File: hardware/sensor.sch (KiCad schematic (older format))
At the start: 55 parts, among them P1 CONN_01X05, SW1 Reset, T1 BUK9Y22, U1 LMR16006, U2 CD74HC4046, U3 CD74HC4046, U4 Atmel_SAM_D09, U5 OPA376AIDCK, X1 UART, X2 60V

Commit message: Finished routing except GND (needs plane etc pp); VCC and maybe even 3V3 needs thicker traces; Fixed missing supply cap for SAMD09 in the schema as well as some wrong footprint for SWD
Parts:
- added C6: 100n, Capacitors_SMD:C_0603, symbol C_Small
- P1: footprint Pin_Headers:Pin_Header_Angled_1x05 -> Connectors_Molex:Connector_Molex_PicoBlade_53261-0571
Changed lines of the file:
@@
 F 0 "P1" H 6500 3150 50  0000 C CNN
 F 1 "CONN_01X05" V 6600 2850 50  0000 C CNN
-F 2 "Pin_Headers:Pin_Header_Angled_1x05" H 6500 2850 50  0001 C CNN
+F 2 "Connectors_Molex:Connector_Molex_PicoBlade_53261-0571" H 6500 2850 50  0001 C CNN
 F 3 "" H 6500 2850 50  0000 C CNN
 	1    6500 2850
@@
 F 3 "" H 8750 2250 50  0000 C CNN
 	1    8750 2250
-	1    0    0    -1
-$EndComp
-$Comp
-L VCC #PWR023
-U 1 1 56E6AE6A
-P 8750 1950
-F 0 "#PWR023" H 8750 1800 50  0001 C CNN
-F 1 "VCC" H 8750 2100 50  0000 C CNN
-F 2 "" H 8750 1950 50  0000 C CNN
-F 3 "" H 8750 1950 50  0000 C CNN
-	1    8750 1950
 	1    0    0    -1
 $EndComp
@@
 	7025 3450 6825 3450
 Connection ~ 6825 3450
+$Comp
+L C_Small C6
+U 1 1 56E7DD7A
+P 7200 1200
+F 0 "C6" H 7210 1270 50  0000 L CNN
+F 1 "100n" H 7210 1120 50  0000 L CNN
+F 2 "Capacitors_SMD:C_0603" H 7200 1200 50  0001 C CNN
+F 3 "" H 7200 1200 50  0000 C CNN
+	1    7200 1200
+	1    0    0    -1
+$EndComp
+$Comp
+L GND #PWR033
+U 1 1 56E7DECB
+P 7200 1300
+F 0 "#PWR033" H 7200 1050 50  0001 C CNN
+F 1 "GND" H 7200 1150 50  0000 C CNN
+F 2 "" H 7200 1300 50  0000 C CNN
+F 3 "" H 7200 1300 50  0000 C CNN
+	1    7200 1300
+	1    0    0    -1
+$EndComp
+$Comp
+L +3V3 #PWR034
+U 1 1 56E7E5A1
+P 7200 1100
+F 0 "#PWR034" H 7200 950 50  0001 C CNN
+F 1 "+3V3" H 7200 1240 50  0000 C CNN
+F 2 "" H 7200 1100 50  0000 C CNN
+F 3 "" H 7200 1100 50  0000 C CNN
+	1    7200 1100
+	1    0    0    -1
+$EndComp
+$Comp
+L +3V3 #PWR?
+U 1 1 56E7F195
+P 8750 1950
+F 0 "#PWR?" H 8750 1800 50  0001 C CNN
+F 1 "+3V3" H 8750 2090 50  0000 C CNN
+F 2 "" H 8750 1950 50  0000 C CNN
+F 3 "" H 8750 1950 50  0000 C CNN
+	1    8750 1950
+	1    0    0    -1
+$EndComp
 $EndSCHEMATC

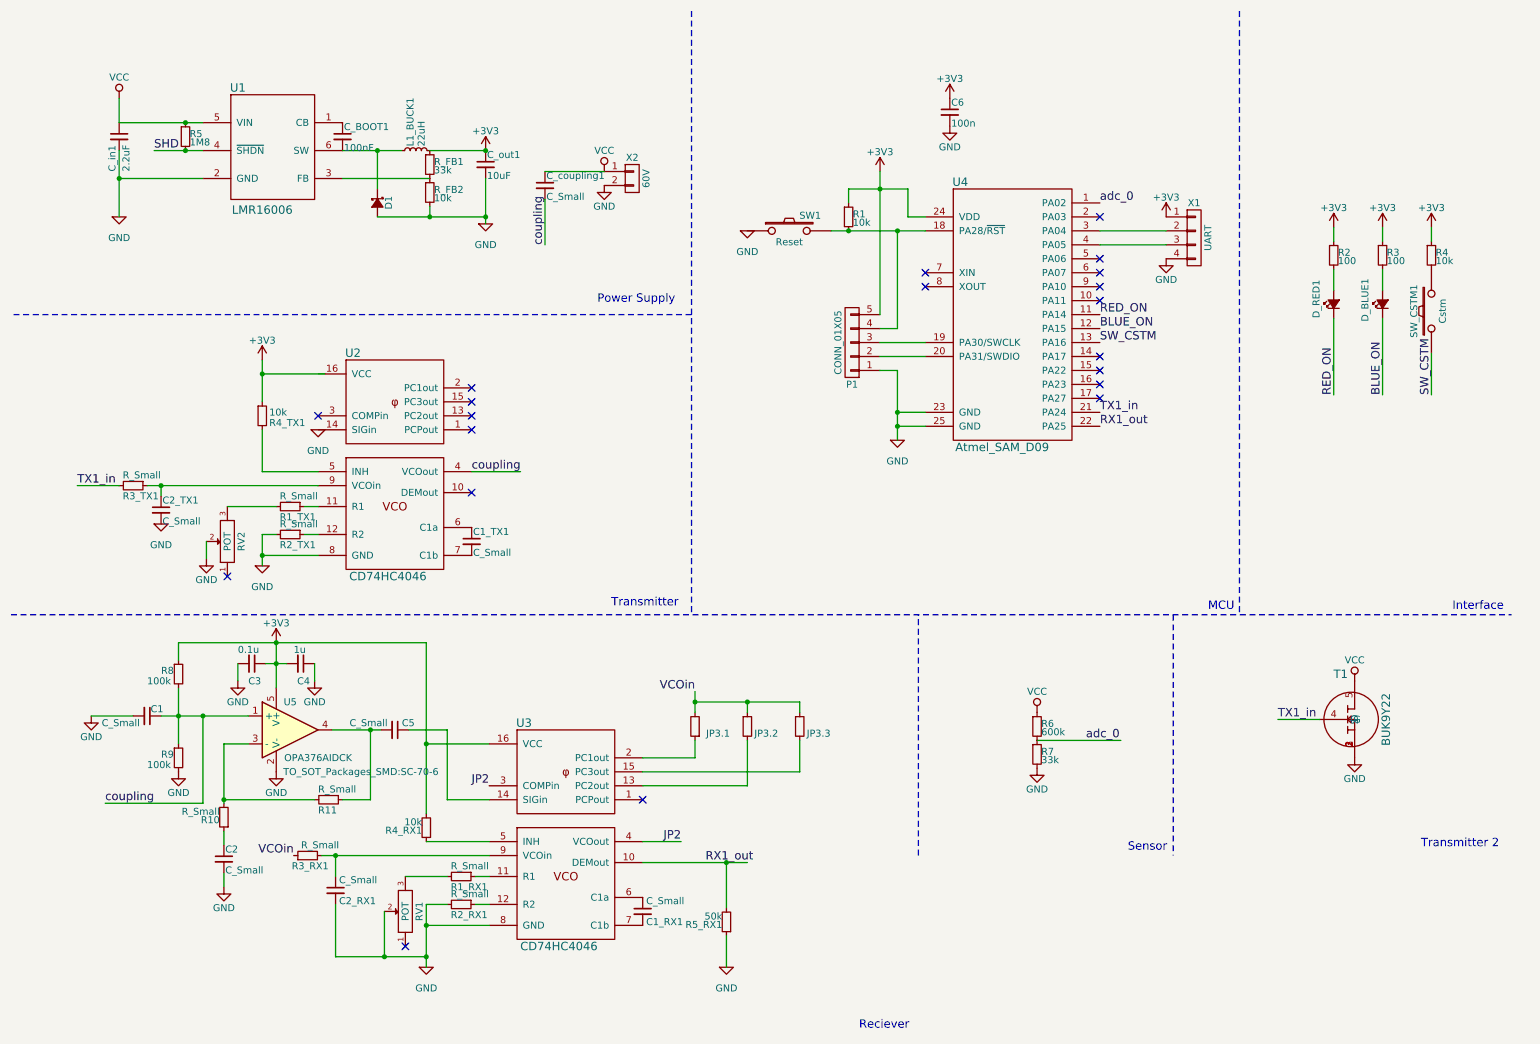
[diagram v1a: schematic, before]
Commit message: Bottom layer labels arranged
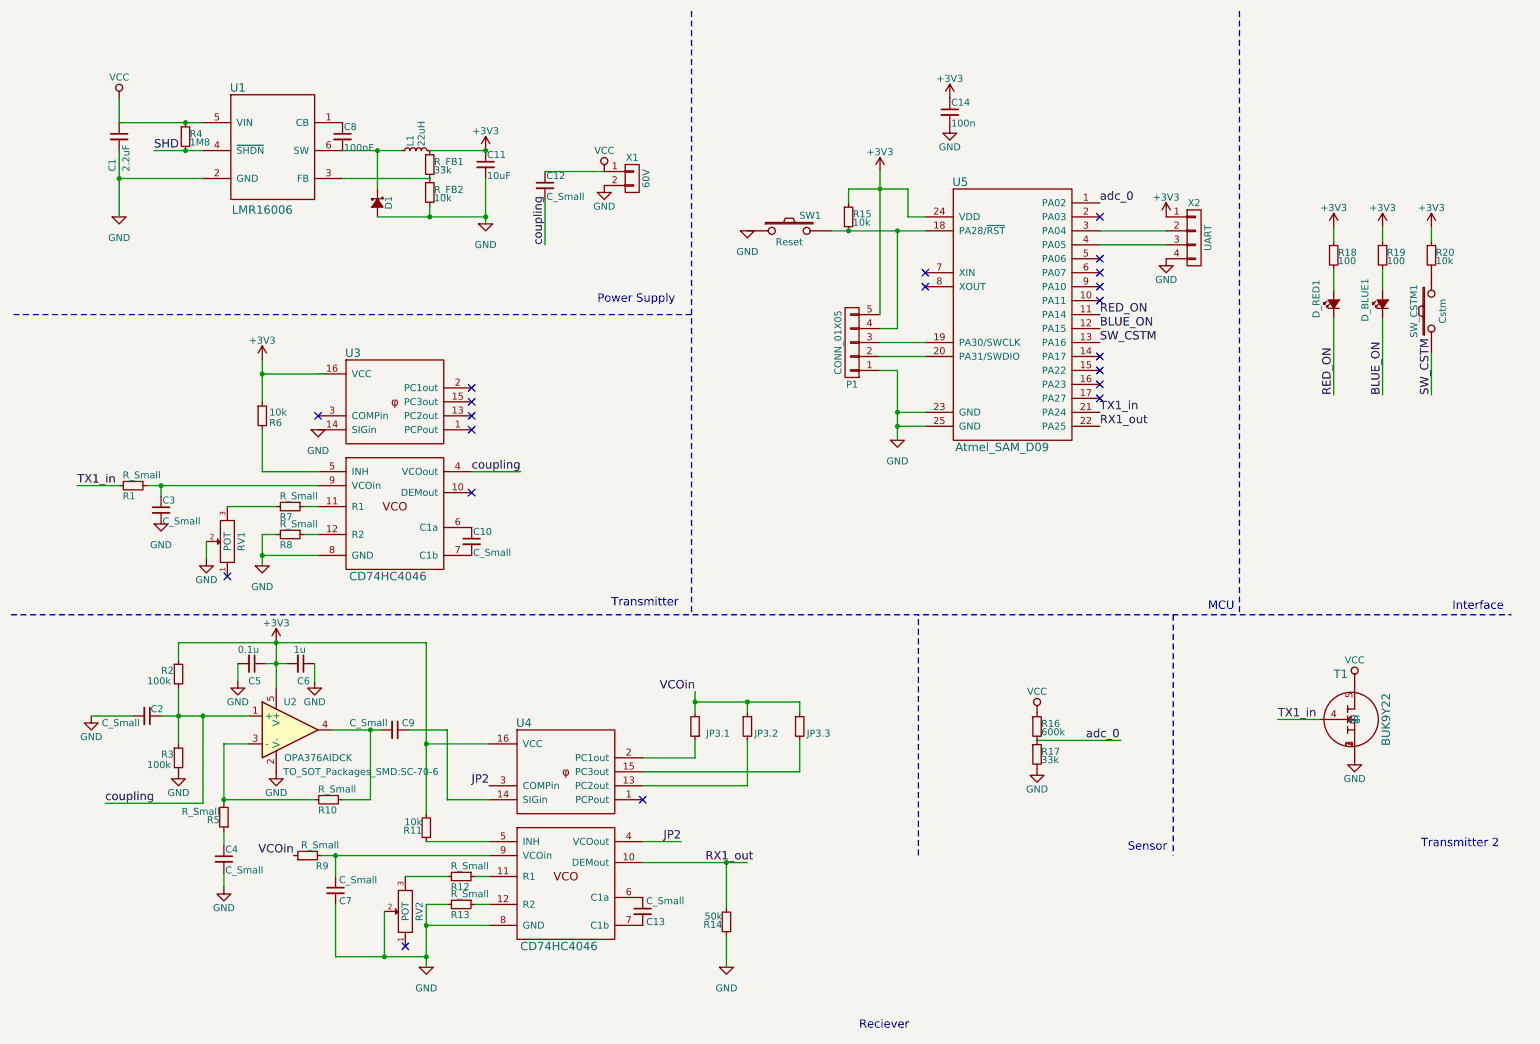
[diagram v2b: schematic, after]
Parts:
- renumbered C_in1 to C1, C1_TX1 to C10, C_out1 to C11, C_coupling1 to C12, C1_RX1 to C13, C6 to C14, C1 to C2, C2_TX1 to C3, C2 to C4, C3 to C5, C4 to C6, C2_RX1 to C7, C_BOOT1 to C8, C5 to C9, L1_BUCK1 to L1, R3_TX1 to R1, R11 to R10, R4_RX1 to R11, R1_RX1 to R12, R2_RX1 to R13, R5_RX1 to R14, R1 to R15, R6 to R16, R7 to R17, R2 to R18, R3 to R19, R8 to R2, R4 to R20, R9 to R3, R5 to R4, R10 to R5, R4_TX1 to R6, R1_TX1 to R7, R2_TX1 to R8, R3_RX1 to R9, RV2 to RV1, RV1 to RV2, U5 to U2, U2 to U3, U3 to U4, U4 to U5, X2 to X1, X1 to X2
